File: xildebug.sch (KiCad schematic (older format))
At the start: 47 parts, among them J1 USB_B_Micro, J2 Conn_STM_SWD, J3 Conn_DUT, J4 Conn_Ext1, J5 Conn_Ext2, J6 Conn_DUT_VDD, U1 STM32L432Kx, U2 XC6206P332MR, U3 MIC5219YMT, U4 MCP4018, U5 MAX14662, U6 TS5A3167, U7 TS5A3167, U8 TS5A3167

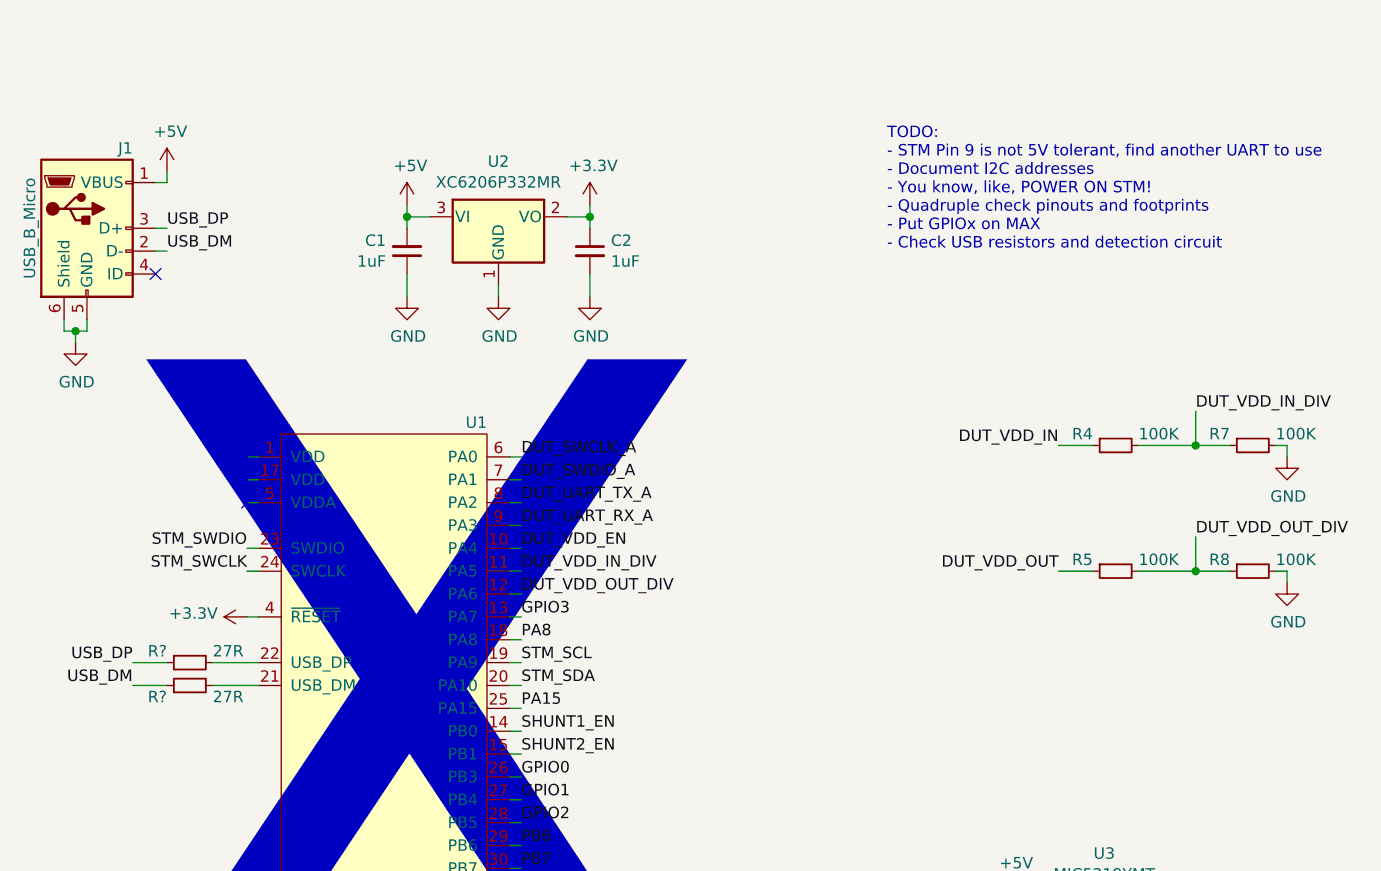
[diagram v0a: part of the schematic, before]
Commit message: Update footprints to nightly
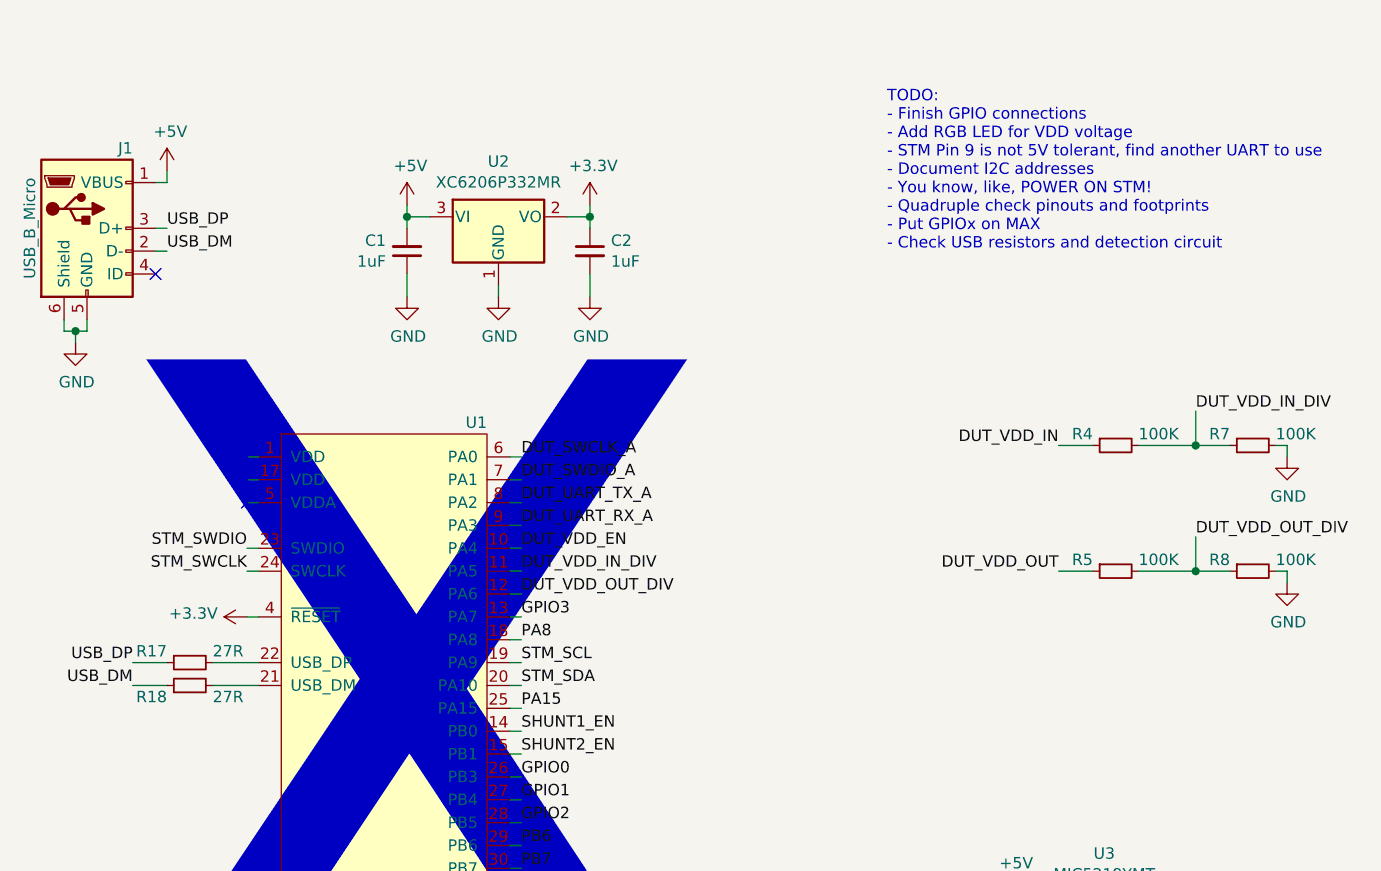
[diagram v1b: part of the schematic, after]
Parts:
- C1, C10, C11, C2, C3, C4, C5, C6, C7, C8, C9: footprint Capacitors_SMD:C_0603 -> Capacitor_SMD:C_0603_1608Metric
- D1, D2: footprint LEDs:LED_0603 -> LED_SMD:LED_0603_1608Metric
- D3, D4: footprint Diodes_SMD:D_SOD-323_HandSoldering -> Diode_SMD:D_SOD-323_HandSoldering
- J1: footprint (none) -> Connector_USB:USB_Micro-B_Molex-105017-0001
- J2: footprint Resistors_SMD:R_0603 -> Connector_PinHeader_2.54mm:PinHeader_1x04_P2.54mm_Vertical
- J3: footprint Resistors_SMD:R_0603 -> Connector_PinHeader_2.54mm:PinHeader_1x06_P2.54mm_Vertical
- J4: footprint Resistors_SMD:R_0603 -> Connector_PinHeader_2.54mm:PinHeader_1x07_P2.54mm_Vertical
- J5: footprint Resistors_SMD:R_0603 -> Connector_PinHeader_2.54mm:PinHeader_1x08_P2.54mm_Vertical
- J6: footprint Pin_Headers:Pin_Header_Angled_1x03_Pitch2.54mm -> Connector_PinHeader_2.54mm:PinHeader_1x03_P2.54mm_Horizontal
- R1, R10, R11, R12, R13, R14, R15, R16, R2, R3, R4, R5, R6, R7, R8, R9: footprint Resistors_SMD:R_0603 -> Resistor_SMD:R_0603_1608Metric
- R17, R18: renamed from R?; footprint Resistors_SMD:R_0603 -> Resistor_SMD:R_0603_1608Metric
- U1: footprint Housings_DFN_QFN:QFN-32-1EP_5x5mm_Pitch0.5mm -> Package_DFN_QFN:QFN-32-1EP_5x5mm_P0.5mm_EP3.45x3.45mm
- U2: footprint Package_TO_SOT_SMD:TSOT-23 -> Package_TO_SOT_SMD:SOT-23
- U3, U6, U7, U8: footprint TO_SOT_Packages_SMD:SOT-23-5 -> Package_TO_SOT_SMD:SOT-23-5
- U4: footprint (none) -> Package_TO_SOT_SMD:SOT-363_SC-70-6
- U5: footprint Housings_DFN_QFN:QFN-28-1EP_4x4mm_Pitch0.4mm -> Package_DFN_QFN:QFN-28-1EP_4x4mm_P0.4mm_EP2.4x2.4mm
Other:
- note added: "TODO:\n- Finish GPIO connections\n- Add RGB LED for VDD voltage\n- STM Pin 9 is not 5V tolerant, find another UART to use\n- Document I2C addresses\n- You know, like, POWER ON STM!\n- Quadruple check pinouts and footprints\n- Put GPIOx on MAX\n- Check USB resistors and detection circuit"
- note removed: "TODO:\n- STM Pin 9 is not 5V tolerant, find another UART to use\n- Document I2C addresses\n- You know, like, POWER ON STM!\n- Quadruple check pinouts and footprints\n- Put GPIOx on MAX\n- Check USB resistors and detection circuit"

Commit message: More work on the schematic
Replaced the STM chip with one that has more GPIO
Added decoupling to STM
Moved VDD circuitry to separate sheet
Added RGB LED
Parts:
- removed C10, C3, C9: 0.1uF, Capacitor_SMD:C_0603_1608Metric, symbol Device:C_Small
- removed R10, R9: TBD, Resistor_SMD:R_0603_1608Metric, symbol Device:R_Small
- removed R11, R12, R13: 10K, Resistor_SMD:R_0603_1608Metric, symbol Device:R_Small
- removed R14: 510R, Resistor_SMD:R_0603_1608Metric, symbol Device:R_Small
- removed R15: 33R, Resistor_SMD:R_0603_1608Metric, symbol Device:R_Small
- removed R16: 1.8R, Resistor_SMD:R_0603_1608Metric, symbol Device:R_Small
- removed R7, R8: 100K, Resistor_SMD:R_0603_1608Metric, symbol Device:R_Small
- removed U1: STM32L432Kx, Package_DFN_QFN:QFN-32-1EP_5x5mm_P0.5mm_EP3.45x3.45mm, symbol MCU_ST_STM32_Extra:STM32L432Kx
- removed U3: MIC5219YMT, Package_TO_SOT_SMD:SOT-23-5, symbol Regulator_Linear_Extra:MIC5219YMT
- removed U4: MCP4018, Package_TO_SOT_SMD:SOT-363_SC-70-6, symbol Potentiometer_Digital_Extra:MCP4018
- removed U6, U7, U8: TS5A3167, Package_TO_SOT_SMD:SOT-23-5, symbol Analog_Switch_Extra:TS5A3167
- added C1, C2: 0.1uF, Capacitor_SMD:C_0603_1608Metric, symbol Device:C_Small
- added C6: 4.7uF, Capacitor_SMD:C_0603_1608Metric, symbol Device:C_Small
- added D1: DUT_UART_TX_LED, LED_SMD:LED_0603_1608Metric, symbol Device:LED_Small
- added D4: LED_RGB, LED_SMD_Extra:LED_RGB_0606_1616Metric, symbol Device_Extra:LED_GRAB
- added R1, R6: 360R, Resistor_SMD:R_0603_1608Metric, symbol Device:R_Small
- added U3: STM32L433CCUx, Package_DFN_QFN:QFN-48-1EP_7x7mm_P0.5mm_EP5.15x5.15mm, symbol MCU_ST_STM32_Extra:STM32L433CCUx
- C11: value 470pF -> 1uF
- C4: value 1uF -> 0.1uF
- C5: value 4.7uF -> 0.1uF
- C7: value 0.1uF -> 10nF
- J3: renamed from J4; footprint Connector_PinHeader_2.54mm:PinHeader_1x07_P2.54mm_Vertical -> Connector_PinHeader_2.54mm:PinHeader_1x11_P2.54mm_Vertical; symbol Connector_Generic:Conn_01x07 -> Connector_Generic:Conn_01x11
- J4: renamed from J5; footprint Connector_PinHeader_2.54mm:PinHeader_1x08_P2.54mm_Vertical -> Connector_PinHeader_2.54mm:PinHeader_1x11_P2.54mm_Vertical; symbol Connector_Generic:Conn_01x08 -> Connector_Generic:Conn_01x11
- R4, R5: value 100K -> 360R
- renumbered C2 to C10, C6 to C3, C1 to C9, D1 to D2, D2 to D3, D3 to D5, D4 to D6, J3 to J5, R6 to R10, R1 to R2, R2 to R3, R18 to R7, R17 to R8, R3 to R9, U2 to U1, U5 to U2
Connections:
- net +3V3: now also C11.1, C4.1, C5.1, C7.1, C8.1, D2.2 (A), D3.2 (A), C1.1, C2.1, C6.1, D1.2 (A), D4.3 (A), U3.1 (VBAT), U3.24 (VDD), U3.36 (VDDUSB), U3.48 (VDD), U3.7 (~RESET~), U3.9 (VDDA); no longer R2.1, R3.1
- net +5V: no longer C4.2, C8.1
- net DUT_SWCLK_A: now also U3.19 (PB1)
- net DUT_SWDIO_A: now also U3.20 (PB2)
- net DUT_UART_RX_A: now also U3.22 (PB11)
- net DUT_UART_RX_LED: now also R3.2, U3.15 (PA5); no longer D3.1 (K)
- net DUT_UART_TX_A: now also U3.21 (PB10)
- net DUT_UART_TX_LED: now also R2.2, U3.14 (PA4); no longer D2.1 (K)
- net DUT_VDD_EN: now also U3.16 (PA6)
- net DUT_VDD_IN: no longer R4.1
- net DUT_VDD_IN_DIV: now also U3.10 (PA0); no longer R4.2
- net DUT_VDD_OUT: no longer R5.1
- net DUT_VDD_OUT_DIV: now also U3.11 (PA1); no longer R5.2
- net DUT_VDD_REG: no longer C5.2, C7.1
- net GND: now also C11.2, C4.2, C5.2, C1.2, C2.2, C6.2, U3.23 (GND), U3.35 (GND), U3.44 (BOOT0), U3.47 (GND), U3.8 (VSSA); no longer C11.1, C4.1, C5.1
- net GPIO0_B: now also U2.17 (B5)
- net GPIO1_B: now also U2.16 (B6)
- net GPIO2_B: now also U2.15 (B7)
- net GPIO3_B: now also U2.14 (B8)
- net PB6: now also J4.10 (Pin_10), U3.42 (PB6); no longer J4.6 (Pin_6)
- net PB7: now also J4.11 (Pin_11), U3.43 (PB7); no longer J4.7 (Pin_7)
- net POT_SCL: now also U3.30 (PA9)
- net POT_SDA: now also U3.31 (PA10)
- net SHUNT1_EN: now also U3.5 (PH0)
- net SHUNT2_EN: now also U3.6 (PH1)
- net STM_SWCLK: now also U3.37 (SWCLK)
- net STM_SWDIO: now also U3.34 (SWDIO)
- net GPIO0_A: now reaches U2.6 (A5)
- net GPIO0_A: now also U3.45 (PB8)
- net GPIO1_A: now reaches U2.7 (A6)
- net GPIO1_A: now also U3.46 (PB9)
- net GPIO2_A: now reaches U2.8 (A7)
- net GPIO2_A: now also U3.2 (PC13)
- net GPIO3_A: now reaches U2.9 (A8)
- net GPIO3_A: now also U3.3 (PC14)
- net at R7.2: now also U3.32 (USB_DM)
- net at R8.2: now also U3.33 (USB_DP)
- net PA15 renamed PA3
- net PA3: now also U3.13 (PA3)
- net PA8 renamed PA2
- net PA2: now also U3.12 (PA2)
- net PH3 renamed PB4
- net PB4: now also U3.40 (PB4)
- new net: D2.1 (K), R2.1
- new net: D3.1 (K), R3.1
- new net: D1.1 (K), R1.1
- new net: D4.1 (GK), R4.1
- new net: D4.2 (RK), R5.1
- new net: D4.4 (BK), R6.1
- new net DUT_SWD_LED: R1.2, U3.18 (PB0)
- new net LED_RGB_B: R6.2, U3.25 (PB12)
- new net LED_RGB_G: R4.2, U3.29 (PA8)
- new net LED_RGB_R: R5.2, U3.38 (PA15)
- new net PA7: J4.6 (Pin_6), U3.17 (PA7)
- new net PB13: J3.8 (Pin_8), U3.26 (PB13)
- new net PB14: J3.9 (Pin_9), U3.27 (PB14)
- new net PB15: J3.10 (Pin_10), U3.28 (PB15)
- new net PB3: J4.7 (Pin_7), U3.39 (PB3)
- new net PB5: J4.9 (Pin_9), U3.41 (PB5)
- new net PC15: J3.11 (Pin_11), U3.4 (PC15)
- no-connect marks 12 -> 1
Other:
- note added: "ADC_IN12"
- note added: "ADC_IN7"
- note added: "ADC_IN8"
- note added: "GPIOs AF"
- note added: "I2C2_SCL"
- note added: "I2C2_SDA"
- note added: "I2C3_SCL"
- note added: "I2C3_SDA"
- note added: "I2C: 0x98"
- note added: "PA15"
- note added: "PA2"
- note added: "PA3"
- note added: "PA7"
- note added: "PB13"
- note added: "PB14"
- note added: "PB15"
- note added: "PB3"
- note added: "PB4"
- note added: "PB5"
- note added: "PB6"
- note added: "PB7"
- note added: "SPI2_MISO"
- note added: "SPI2_MOSI"
- note added: "SPI2_SCK"
- note added: "SPI3_CS"
- note added: "SPI3_MISO"
- note added: "SPI3_MOSI"
- note added: "SPI3_SCK"
- note added: "TODO:\n- Quadruple check pinouts and footprints\n- Check USB detection circuit"
- note added: "USART1_RX"
- note added: "USART1_TX"
- note added: "USART2_RX"
- note added: "USART2_TX"
- note removed: "GPIO AF:\nGPIO0 - SPI3_CLK\nGPIO1 - SPI3_MISO/I2C3_SDA\nGPIO2 - SPI3_MOSI\nGPIO3 - SPI3_CS/I2C3_SCL/ADC_IN12"
- note removed: "TODO:\n- Finish GPIO connections\n- Add RGB LED for VDD voltage\n- STM Pin 9 is not 5V tolerant, find another UART to use\n- Document I2C addresses\n- You know, like, POWER ON STM!\n- Quadruple check pinouts and footprints\n- Put GPIOx on MAX\n- Check USB resistors and detection circuit"
- note removed: "X"
- moved on the sheet: C10, C3, C9, D2, D3, D5, D6, J1, J2, J5, J6, R10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
